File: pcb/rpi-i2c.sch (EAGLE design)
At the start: 14 parts, among them IC1 DS2482-100, J2 CONN_05X2

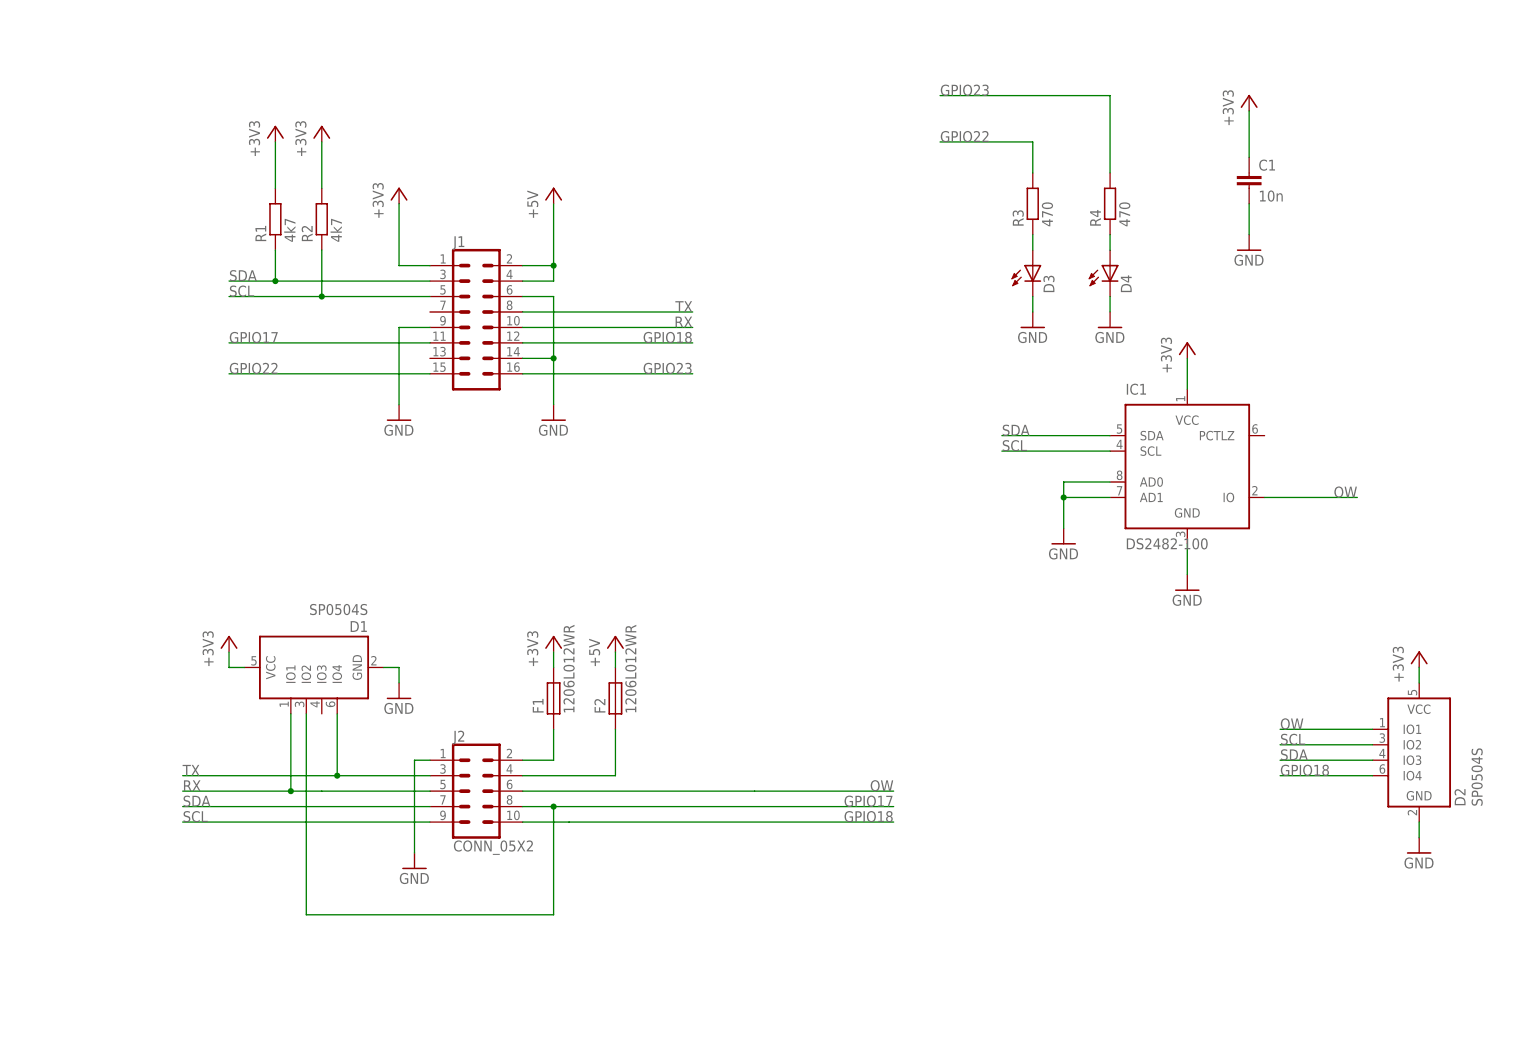
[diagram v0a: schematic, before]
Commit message: Clean up schematics and save PCB image.
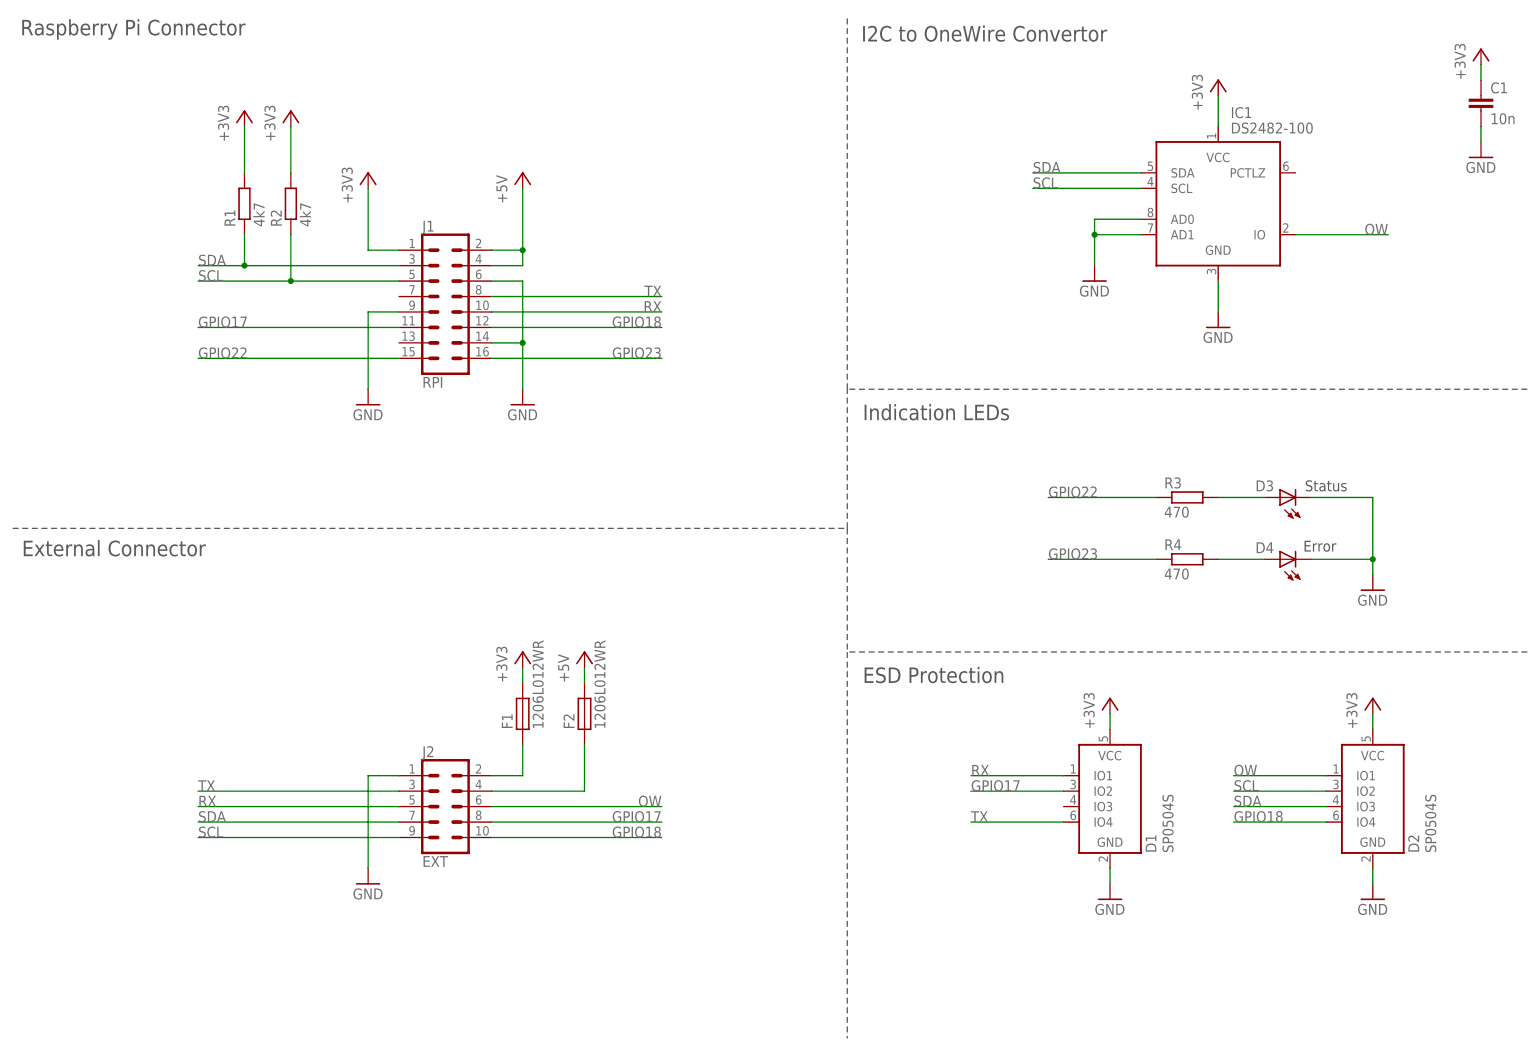
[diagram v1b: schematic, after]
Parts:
- J1: value (none) -> RPI
- J2: value CONN_05X2 -> EXT
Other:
- note added: "ESD Protection"
- note added: "Error"
- note added: "External Connector"
- note added: "I2C to OneWire Convertor"
- note added: "Indication LEDs"
- note added: "Raspberry Pi Connector"
- note added: "Status"
- moved on the sheet: C1, D1, D2, D3, D4, F1, F2, IC1, J1, J2, R1, R2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
